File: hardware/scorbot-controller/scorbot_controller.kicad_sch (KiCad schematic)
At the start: 102 parts, among them J1 12V in (CUI PJ-102AH, 2.1 mm), J2 12V in (screw terminal, +/-), J3 E-STOP (NC, in VM line), J4 DD-50 female R/A (robot cable), J5 I2C expansion, J6 Spare TCA9555 I/O, J7 FUSE alt: wire inline 5A fuse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, U1 DROK mini buck, set to 5V, U10 Pololu #4035 DRV8874 (M1), U11 Pololu #4035 DRV8874 (M2), U12 Pololu #4035 DRV8874 (M3), U13 Pololu #4035 DRV8874 (M4), U14 Pololu #4035 DRV8874 (M5), U15 Pololu #4035 DRV8874 (M6), U2 ESP32-DevKitC (WROOM-32D or -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, U5 TCA9555PWR (0x20), U6 ADS1115IDGSR (0x48), U7 ADS1115IDGSR (0x49)

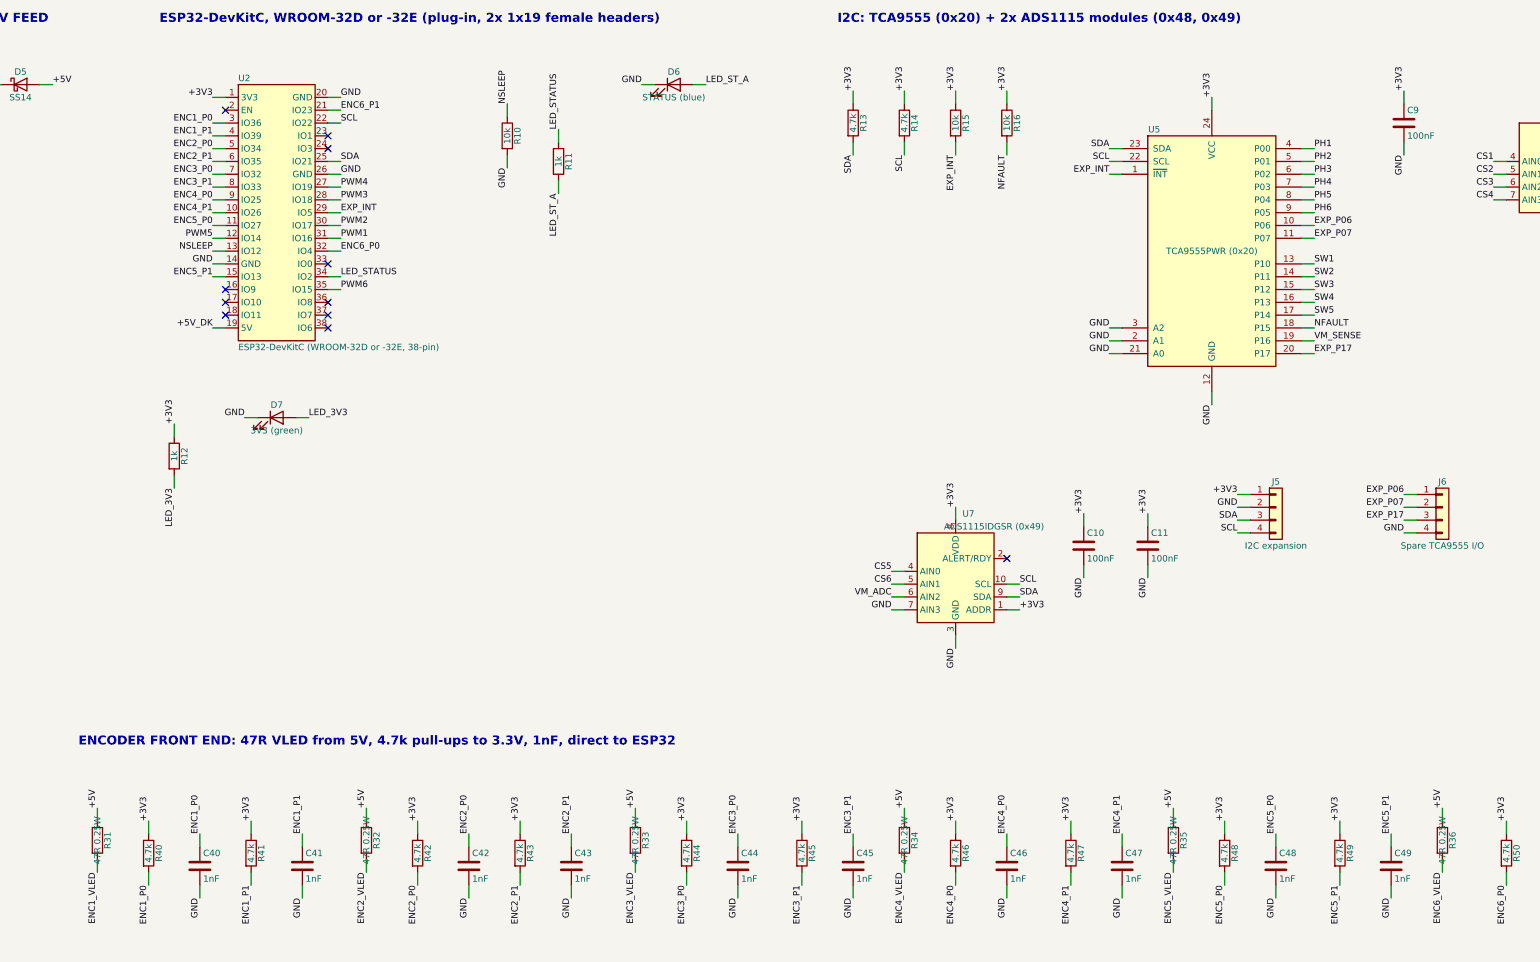
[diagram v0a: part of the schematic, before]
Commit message: v0.4: DD-50 footprint per Amphenol DD50S564TLF, logos on silkscreen, LCSC fixes
- DD-50: tail rows 2.54 mm apart, row 3 10.40 mm from the flange (Amphenol
  D-Sub brochure, termination type 5); bracket holes still to confirm
- Columbia Gadget Works logo on F.SilkS, Stealie on B.SilkS (silk_art.py)
- R31-R36 47R now 2512 1 W (~0.3 W each); D6 status LED red (C84256)
- Clear LCSC numbers that turned out wrong (TCA9555, 47R); previews draw silk on top

Co-Authored-By: Claude Opus 5.5 <noreply@anthropic.com>
Claude-Session: https://claude.ai/code/session_01EVE6PZ95cMufMkAr9pDFuN
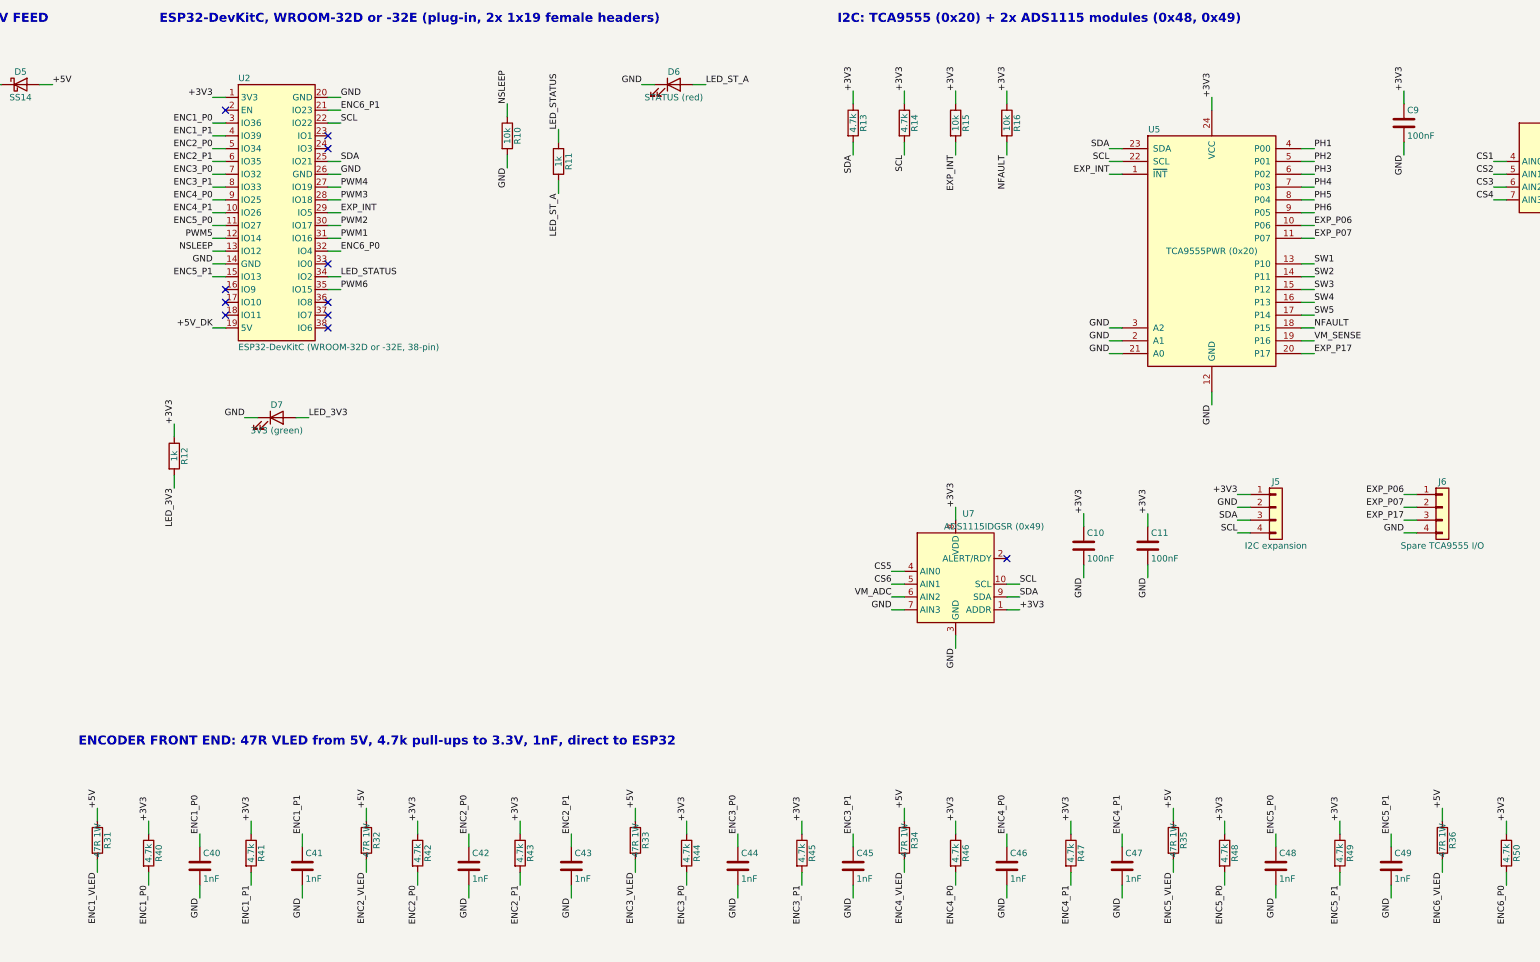
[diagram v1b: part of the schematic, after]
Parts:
- D6: value STATUS (blue) -> STATUS (red)
- J4: footprint Scorbot:DD50_Female_Horizontal_P2.77x2.84mm -> Scorbot:DD50_Female_Horizontal_P2.77x2.54mm_EdgePinOffset10.40mm
- R31, R32, R33, R34, R35, R36: value 47R 0.25W -> 47R 1W; footprint Resistor_SMD:R_1206_3216Metric -> Resistor_SMD:R_2512_6332Metric
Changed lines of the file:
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@@
       (effects (font (size 1.27 1.27)))
     )
-    (property "Value" "STATUS (blue)" (id 1) (at 452.12 35.56 0)
+    (property "Value" "STATUS (red)" (id 1) (at 452.12 35.56 0)
       (effects (font (size 1.27 1.27)))
     )
@@
       (effects (font (size 1.27 1.27)))
     )
-    (property "Value" "47R 0.25W" (id 1) (at 337.82 182.88 90)
-      (effects (font (size 1.27 1.27)))
-    )
-    (property "Footprint" "Resistor_SMD:R_1206_3216Metric" (id 2) (at 336.04 182.88 90)
+    (property "Value" "47R 1W" (id 1) (at 337.82 182.88 90)
+      (effects (font (size 1.27 1.27)))
+    )
+    (property "Footprint" "Resistor_SMD:R_2512_6332Metric" (id 2) (at 336.04 182.88 90)
       (effects (font (size 1.27 1.27)) hide)
     )
@@
       (effects (font (size 1.27 1.27)))
     )
-    (property "Value" "47R 0.25W" (id 1) (at 391.16 182.88 90)
-      (effects (font (size 1.27 1.27)))
-    )
-    (property "Footprint" "Resistor_SMD:R_1206_3216Metric" (id 2) (at 389.38 182.88 90)
+    (property "Value" "47R 1W" (id 1) (at 391.16 182.88 90)
+      (effects (font (size 1.27 1.27)))
+    )
+    (property "Footprint" "Resistor_SMD:R_2512_6332Metric" (id 2) (at 389.38 182.88 90)
       (effects (font (size 1.27 1.27)) hide)
     )
@@
       (effects (font (size 1.27 1.27)))
     )
-    (property "Value" "47R 0.25W" (id 1) (at 444.5 182.88 90)
-      (effects (font (size 1.27 1.27)))
-    )
-    (property "Footprint" "Resistor_SMD:R_1206_3216Metric" (id 2) (at 442.72 182.88 90)
+    (property "Value" "47R 1W" (id 1) (at 444.5 182.88 90)
+      (effects (font (size 1.27 1.27)))
+    )
+    (property "Footprint" "Resistor_SMD:R_2512_6332Metric" (id 2) (at 442.72 182.88 90)
       (effects (font (size 1.27 1.27)) hide)
     )
@@
       (effects (font (size 1.27 1.27)))
     )
-    (property "Value" "47R 0.25W" (id 1) (at 497.84 182.88 90)
-      (effects (font (size 1.27 1.27)))
-    )
-    (property "Footprint" "Resistor_SMD:R_1206_3216Metric" (id 2) (at 496.06 182.88 90)
+    (property "Value" "47R 1W" (id 1) (at 497.84 182.88 90)
+      (effects (font (size 1.27 1.27)))
+    )
+    (property "Footprint" "Resistor_SMD:R_2512_6332Metric" (id 2) (at 496.06 182.88 90)
       (effects (font (size 1.27 1.27)) hide)
     )
@@
       (effects (font (size 1.27 1.27)))
     )
-    (property "Value" "47R 0.25W" (id 1) (at 551.18 182.88 90)
-      (effects (font (size 1.27 1.27)))
-    )
-    (property "Footprint" "Resistor_SMD:R_1206_3216Metric" (id 2) (at 549.4 182.88 90)
+    (property "Value" "47R 1W" (id 1) (at 551.18 182.88 90)
+      (effects (font (size 1.27 1.27)))
+    )
+    (property "Footprint" "Resistor_SMD:R_2512_6332Metric" (id 2) (at 549.4 182.88 90)
       (effects (font (size 1.27 1.27)) hide)
     )
@@
       (effects (font (size 1.27 1.27)))
     )
-    (property "Value" "47R 0.25W" (id 1) (at 604.52 182.88 90)
-      (effects (font (size 1.27 1.27)))
-    )
-    (property "Footprint" "Resistor_SMD:R_1206_3216Metric" (id 2) (at 602.74 182.88 90)
+    (property "Value" "47R 1W" (id 1) (at 604.52 182.88 90)
+      (effects (font (size 1.27 1.27)))
+    )
+    (property "Footprint" "Resistor_SMD:R_2512_6332Metric" (id 2) (at 602.74 182.88 90)
       (effects (font (size 1.27 1.27)) hide)
     )
@@
       (effects (font (size 1.27 1.27)) (justify left))
     )
-    (property "Footprint" "Scorbot:DD50_Female_Horizontal_P2.77x2.84mm" (id 2) (at 45.72 292.1 0)
-      (effects (font (size 1.27 1.27)) hide)
-    )
+    (property "Footprint" "Scorbot:DD50_Female_Horizontal_P2.77x2.54mm_EdgePinOffset10.40mm" (id 2) (at 45.72 292.1 0)
+      (effects (font (size 1.27 1.27)) hide)
+    )
